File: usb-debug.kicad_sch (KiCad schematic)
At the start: 81 parts, among them IC15 TPS7A0518PDBVT, IC16 AP22653W6-7, IC7 HD3SS3220, J11 632723300011, T6 BSS138APW, T7 BSS138APW

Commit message: Add some todos
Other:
- note added: "TODO: Add 0R here"
- note added: "TODO: check that - remove if possible"
- note added: "TODO: simulate the actual OTG function by driving the ID pin"
- note added: "TODO: use another driver to deliver power to VBUS while in host mode"
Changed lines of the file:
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@@
     )
+  )
+  (text "TODO: use another driver to deliver power to VBUS while in host mode"
+    (at 213.36 152.4 0)
+    (effects (font (size 1.27 1.27)) (justify left bottom))
   )
   (text "USB-OTG" (at 160.655 135.89 0)
@@
     (effects (font (size 1.4986 1.4986) (thickness 0.2997) bold) (justify left bottom))
   )
+  (text "TODO: check that - remove if possible" (at 168.91 132.08 0)
+    (effects (font (size 1.27 1.27)) (justify left bottom))
+  )
   (text "Both DNP - GPIO Mode\nHIGH - I2C Mode 0x67\nLOW -  I2C Mode 0x47"
     (at 35.56 120.015 0)
+    (effects (font (size 1.27 1.27)) (justify left bottom))
+  )
+  (text "TODO: simulate the actual OTG function\nby driving the ID pin"
+    (at 213.36 145.415 0)
     (effects (font (size 1.27 1.27)) (justify left bottom))
   )
@@
     (effects (font (size 0.9906 0.9906)) (justify left bottom))
   )
+  (text "TODO: Add 0R here" (at 122.555 138.43 0)
+    (effects (font (size 1.27 1.27)) (justify left bottom))
+  )
   (text "Text" (at 67.7926 1253.8202 0)

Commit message: Resolve TOOD on USB sheet
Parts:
- removed D9: PESD2USB5UV-TR, jetson-nano-baseboard-footprints:SOT-23s, symbol jetson-nano-baseboard:PESD2USB5UV-TR
- removed Q? (x2): PMV32UP, jetson-nano-baseboard-footprints:SOT-23s, symbol jetson-nano-baseboard:PMOS
- removed R71: R_0R_0402, jetson-nano-baseboard-footprints:0402-res, symbol jetson-nano-baseboard:R_0R_0402
- removed R?: R_10k_0402, jetson-nano-baseboard-footprints:0402-res, symbol jetson-nano-baseboard:R_10k_0402
- removed T?: BSS138APW, jetson-nano-baseboard-footprints:SC70-3, symbol jetson-nano-baseboard:BSS138APW
- added IC1: AP22652W6-7, antmicro-footprints:SOT-23-6, symbol antmicroPMICPowerDistributionSwitchesLoadDrivers:AP22652W6-7
- added L11: BLM18SG121TN1D, jetson-nano-baseboard-footprints:0603, symbol jetson-nano-baseboard:BLM18SG121TN1D
- added LED2: ~, jetson-nano-baseboard-footprints:LED0603, symbol jetson-nano-baseboard:LED
- added R129, R136: R_0R_0402, jetson-nano-baseboard-footprints:0402-res, symbol jetson-nano-baseboard:R_0R_0402
- added R133, R134: R_10k_0402, jetson-nano-baseboard-footprints:0402-res, symbol jetson-nano-baseboard:R_10k_0402
- added R135: R_470R_0402, jetson-nano-baseboard-footprints:0402-res, symbol jetson-nano-baseboard:R_470R_0402
- added R138: R_12k4_0402, jetson-nano-baseboard-footprints:0402-res, symbol jetson-nano-baseboard:R_12k4_0402
- added T10, T9: BSS138APW, jetson-nano-baseboard-footprints:SC70-3, symbol jetson-nano-baseboard:BSS138APW
- gave numbers to parts that had none: 5
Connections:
- net 5V0_SYS: now also IC1.1 (IN), R134.2, R135.2, R136.1
- net GND: now also IC1.2 (GND), R138.1
- net OTG_USB_VBUS: now also C62.2, J5.1 (VCC), R72.1, L11.2 (P); no longer T6.3 (D)
- net USBC_VBUS: no longer R42.2
- net at C31.2, IC16.6 (OUT), L2.1 (P): now also R42.2
- net USB_DBG_VBUS: now reaches J9.1 (VCC), L3.1 (P)
- net OTG_ID_5V renamed OTG_USB_ID
- net OTG_USB_ID: now also IC1.3 (~{EN}), R134.1, T10.3 (D), T9.1 (G)
- new net: R129.1, T6.3 (D), T9.2 (S)
- new net: IC1.5 (ILIM), R138.2
- new net: IC1.6 (OUT), L11.1 (P), R136.2
- new net: LED2.A, R135.1
- new net 1V8_SYS: R133.1, T10.1 (G)
- new net ~{OTG_USB_FAULT}: IC1.4 (~{FAULT}), LED2.K
- new net ~{OTG_USB_ID_DET}: R133.2, T10.2 (S)
- new net ~{OTG_USB_VBUS_DET}: R129.2, T9.3 (D)
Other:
- note added: "DISC HOST DEVICE"
- note added: "HIGH LOW HIGH"
- note added: "HIGH-Z HIGH-Z LOW"
- note added: "ID"
- note added: "ID/VBUS DET signals"
- note added: "ID_DET"
- note added: "LOW HIGH HIGH"
- note added: "OTG TRUTH TABLE"
- note added: "OTG/Flash USB"
- note added: "STATE"
- note added: "USB-C Load Switch"
- note added: "VBUS"
- note added: "VBUS_DET"
- note removed: "TODO: Add 0R here"
- note removed: "TODO: check that - remove if possible"
- note removed: "TODO: simulate the actual OTG function by driving the ID pin"
- note removed: "TODO: use another driver to deliver power to VBUS while in host mode"
- note removed: "USB Load Switch"
- note removed: "USB-OTG"
- moved on the sheet: C15, C29, C30, C31, C32, C35, C62, C66, C67, C72, D17, D3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

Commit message: Continue placement, mix USB SS signals as HD3SS3220 allows for it
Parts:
- removed D8: PESD2USB5UV-TR, jetson-nano-baseboard-footprints:SOT-23s, symbol jetson-nano-baseboard:PESD2USB5UV-TR
- added D8: TPD4E05U06_PASS, jetson-nano-baseboard-footprints:TPD4E05U06_PASS, symbol jetson-nano-baseboard:TPD4E05U06_PASS
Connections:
- net C_USBSS_TX1_N: now also C50.1; no longer C48.1
- net C_USBSS_TX1_P: now also C48.1; no longer C50.1
- net C_USBSS_TX2_N: now also C54.1, D7.1 (CH1); no longer C53.1, D7.2 (CH2)
- net C_USBSS_TX2_P: now also C53.1, D7.2 (CH2); no longer C54.1, D7.1 (CH1)
- net GND: now also D8.3 (GND), D8.8 (GND)
- net OTG_USB_D_N: now also D8.1 (CH1)
- net OTG_USB_D_P: now also D8.2 (CH2)
- net OTG_USB_ID: now also D8.4 (CH3)
- net USBSS_TX1_N: now also C50.2, IC7.17 (TX1p); no longer C48.2, IC7.16 (TX1n)
- net USBSS_TX1_P: now also C48.2, IC7.16 (TX1n); no longer C50.2, IC7.17 (TX1p)
- net USBSS_TX2_N: now also C54.2, IC7.21 (TX2p); no longer C53.2, IC7.20 (TX2n)
- net USBSS_TX2_P: now also C53.2, IC7.20 (TX2n); no longer C54.2, IC7.21 (TX2p)
- net ~{OTG_USB_FAULT}: now also LED2.2 (K); no longer LED2.K
- net at R43.1: now also LED1.1 (A); no longer LED1.A
- net at IC16.4 (~{FAULT}): now also LED1.2 (K); no longer LED1.K
- net at R135.1: now also LED2.1 (A); no longer LED2.A
- no-connect marks 16 -> 17

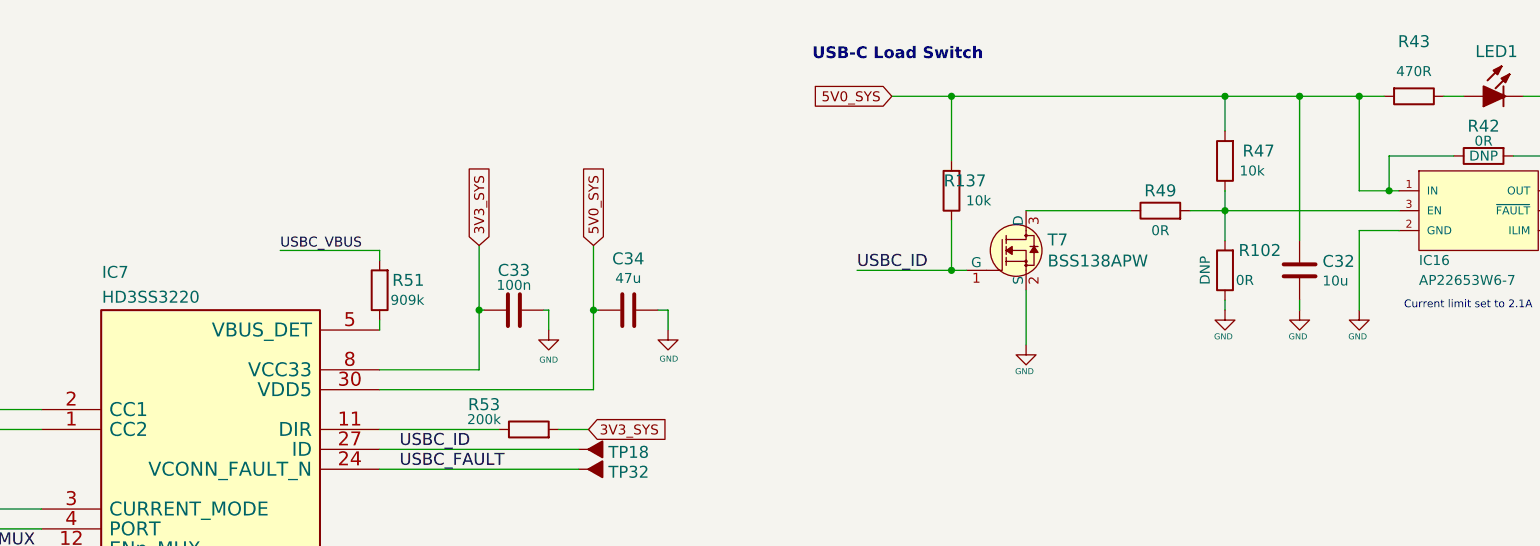
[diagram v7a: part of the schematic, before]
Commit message: Improve USB-C load switch ctrl circuit
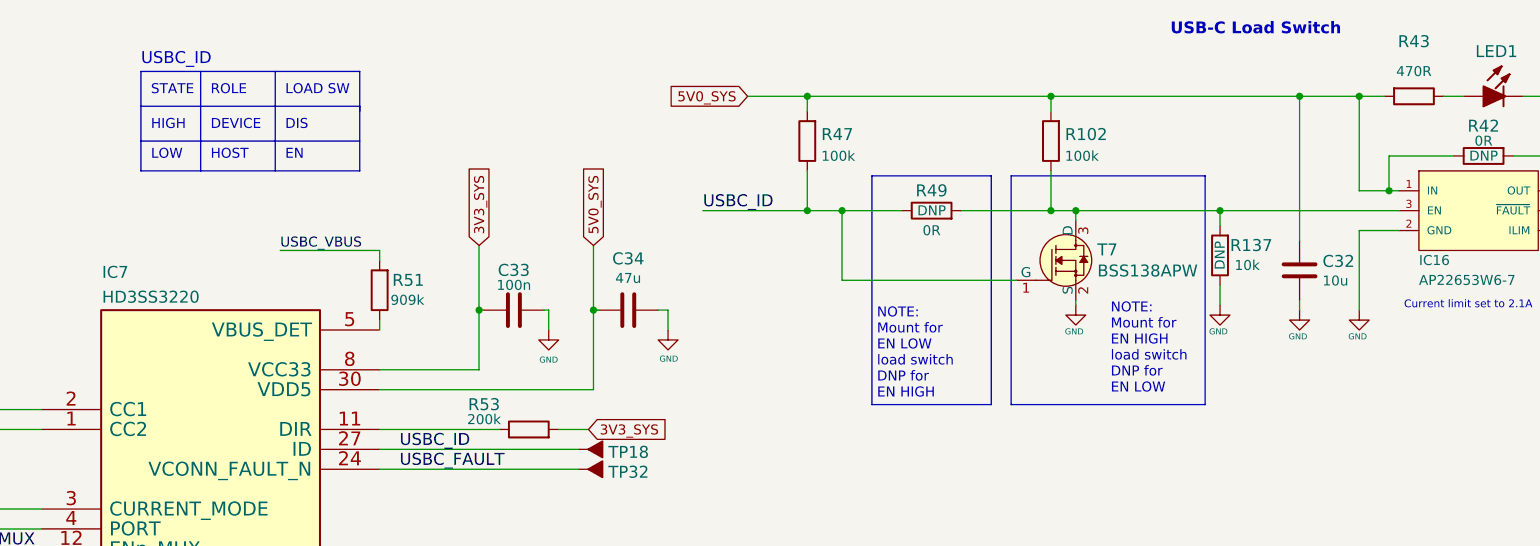
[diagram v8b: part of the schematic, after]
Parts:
- removed R102: R_0R_0402, jetson-nano-baseboard-footprints:0402-res, symbol jetson-nano-baseboard:R_0R_0402
- removed R47: R_10k_0402, jetson-nano-baseboard-footprints:0402-res, symbol jetson-nano-baseboard:R_10k_0402
- added R102, R47: R_100k_0402, jetson-nano-baseboard-footprints:0402-res, symbol jetson-nano-baseboard:R_100k_0402
- R137, R49: DNP (none) -> DNP
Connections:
- net 5V0_SYS: now also R102.2, R47.2; no longer R137.2
- net GND: now also R137.1
- net USBC_ID: now also R49.1, R47.1; no longer R137.1
- net at T7.3 (D): now also IC16.3 (EN), R137.2, R49.2, R102.1; no longer R49.1
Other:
- note added: "DEVICE"
- note added: "DIS"
- note added: "EN"
- note added: "HIGH"
- note added: "HOST"
- note added: "LOAD SW"
- note added: "LOW"
- note added: "NOTE: Mount for EN HIGH load switch DNP for EN LOW"
- note added: "NOTE: Mount for EN LOW load switch DNP for EN HIGH"
- note added: "ROLE"
- note added: "USBC_ID"
- moved on the sheet: T7
